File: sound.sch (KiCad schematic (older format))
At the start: 16 parts, among them Q2 2SC1815, U5 6581

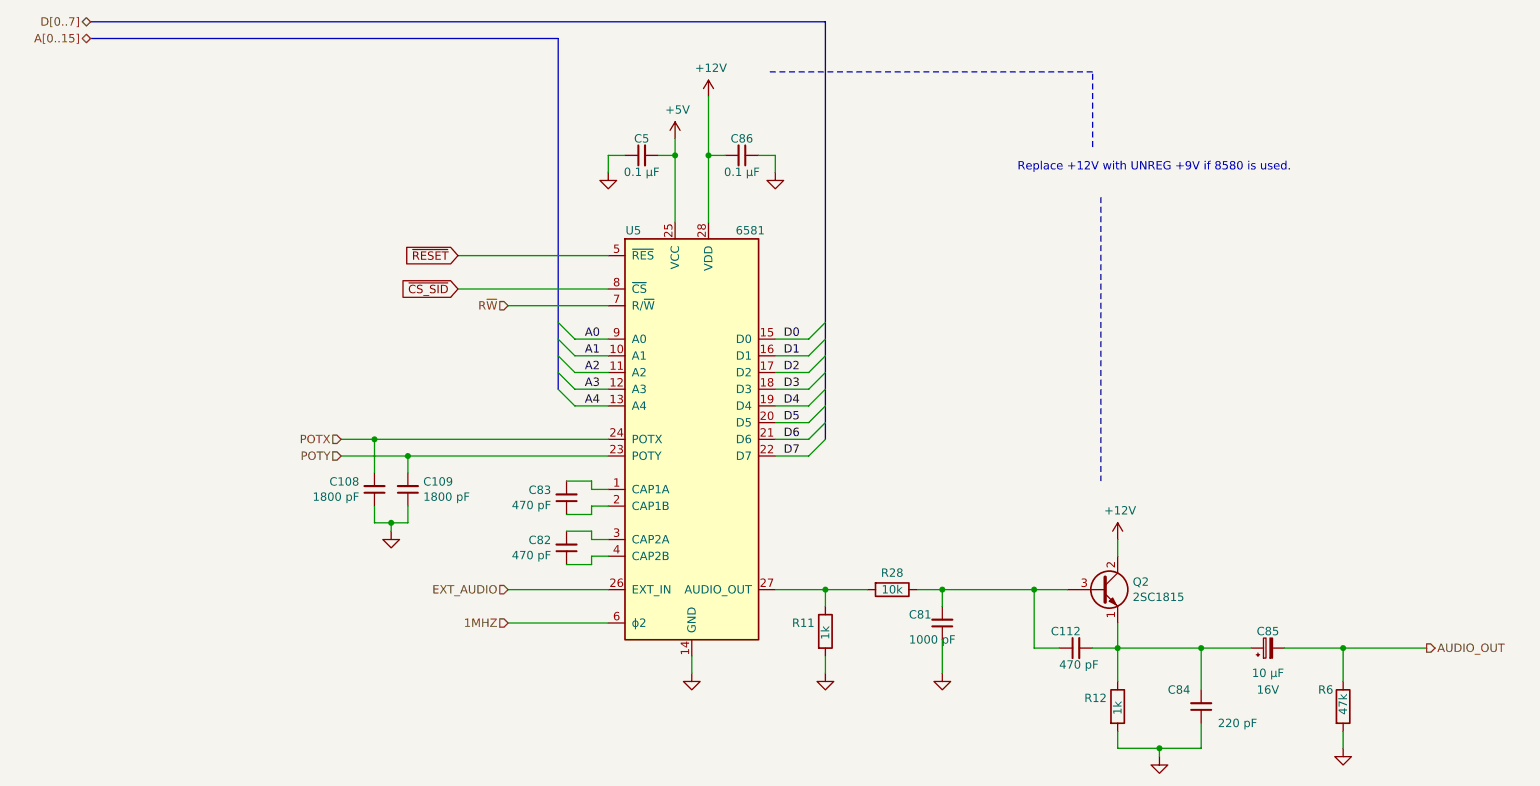
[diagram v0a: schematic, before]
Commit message: Clean up schematic
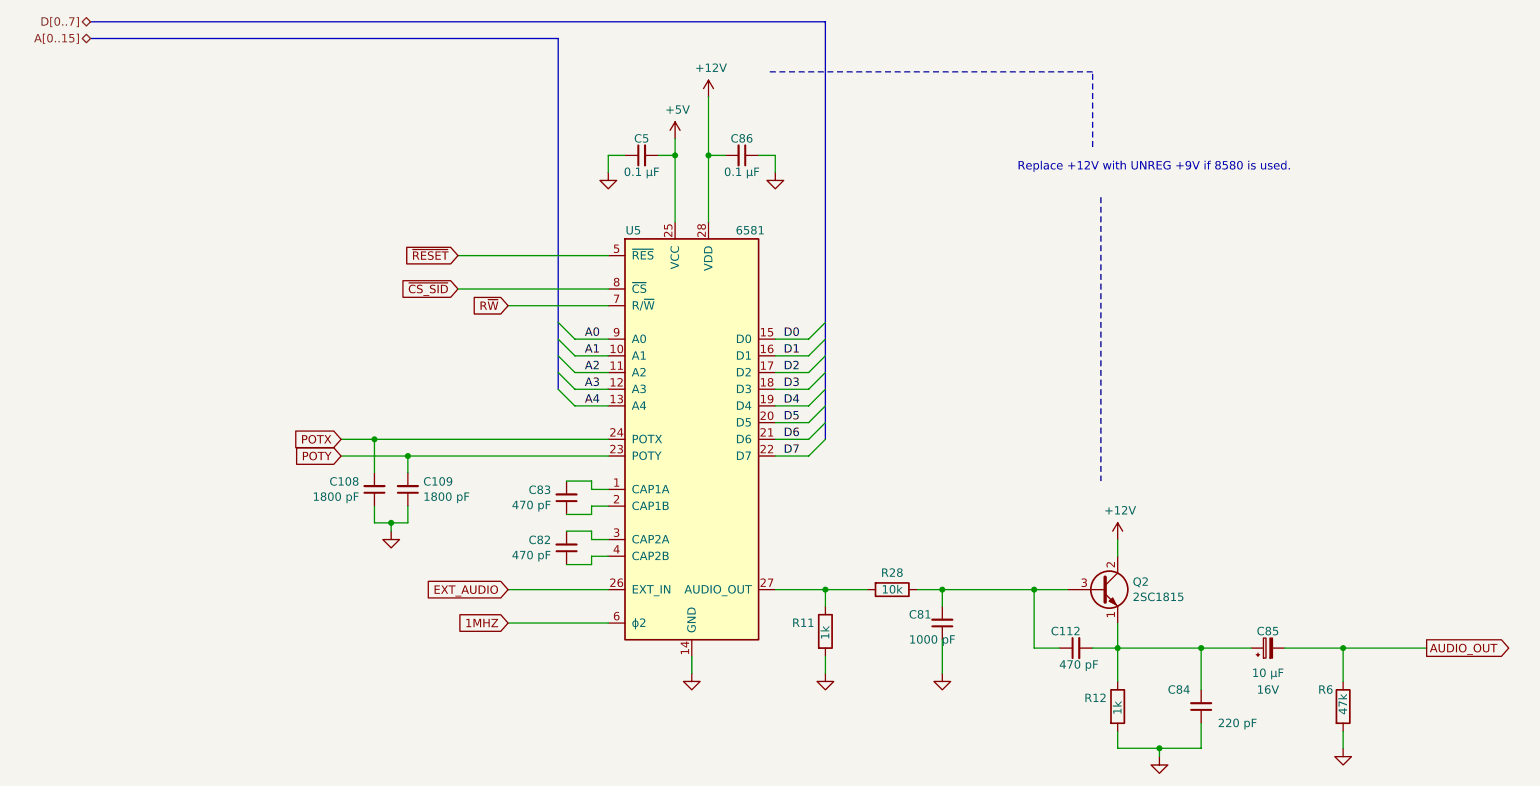
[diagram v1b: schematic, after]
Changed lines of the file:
@@
 Text HLabel 1000 1250 0    50   BiDi ~ 0
 A[0..15]
-Text HLabel 3500 2850 0    50   Input ~ 0
-R~W
-Text HLabel 3500 4550 0    50   Input ~ 0
-EXT_AUDIO
-Text HLabel 3500 4750 0    50   Input ~ 0
-1MHZ
 Wire Wire Line
 	3200 2550 4100 2550
@@
 Wire Wire Line
 	4000 4350 4100 4350
-Text HLabel 2500 3650 0    50   Input ~ 0
-POTX
-Text HLabel 2500 3750 0    50   Input ~ 0
-POTY
 Wire Wire Line
 	2500 3650 2700 3650
@@
 Wire Wire Line
 	8500 4900 8500 5100
-Text HLabel 9000 4900 2    50   Output ~ 0
-AUDIO_OUT
 Wire Wire Line
 	8500 4900 9000 4900
@@
 Wire Bus Line
 	5400 1150 5400 3650
+Text GLabel 3500 2850 0    50   Input ~ 0
+R~W
+Text GLabel 3500 4750 0    50   Input ~ 0
+1MHZ
+Text GLabel 9000 4900 2    50   Output ~ 0
+AUDIO_OUT
+Text GLabel 3500 4550 0    50   Input ~ 0
+EXT_AUDIO
+Text GLabel 2500 3650 0    50   Input ~ 0
+POTX
+Text GLabel 2500 3750 0    50   Input ~ 0
+POTY
 $EndSCHEMATC
